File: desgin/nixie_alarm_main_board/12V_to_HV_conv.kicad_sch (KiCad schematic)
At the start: 23 parts, among them IC1 LM3488MM, IC8 MCP4018T-502E_LT, Q8 TPH5200FNH,L1Q

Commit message: koncepcja układu
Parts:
- IC8: value MCP4018T-502E_LT -> MCP4018T-103E/LT
- R44: value 27kΩ -> 35.7kΩ
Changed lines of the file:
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@@
 			)
 		)
-		(property "Value" "MCP4018T-502E_LT"
+		(property "Value" "MCP4018T-103E/LT"
 			(at 45.72 104.14 0)
 			(effects
@@
 			)
 		)
-		(property "Description" "5kΩ 7-bit"
+		(property "Description" "10kΩ 7-bit"
 			(at 45.974 118.872 0)
 			(effects
@@
 			)
 		)
-		(property "Value" "27kΩ"
+		(property "Value" "35.7kΩ"
 			(at 158.75 109.22 90)
 			(effects

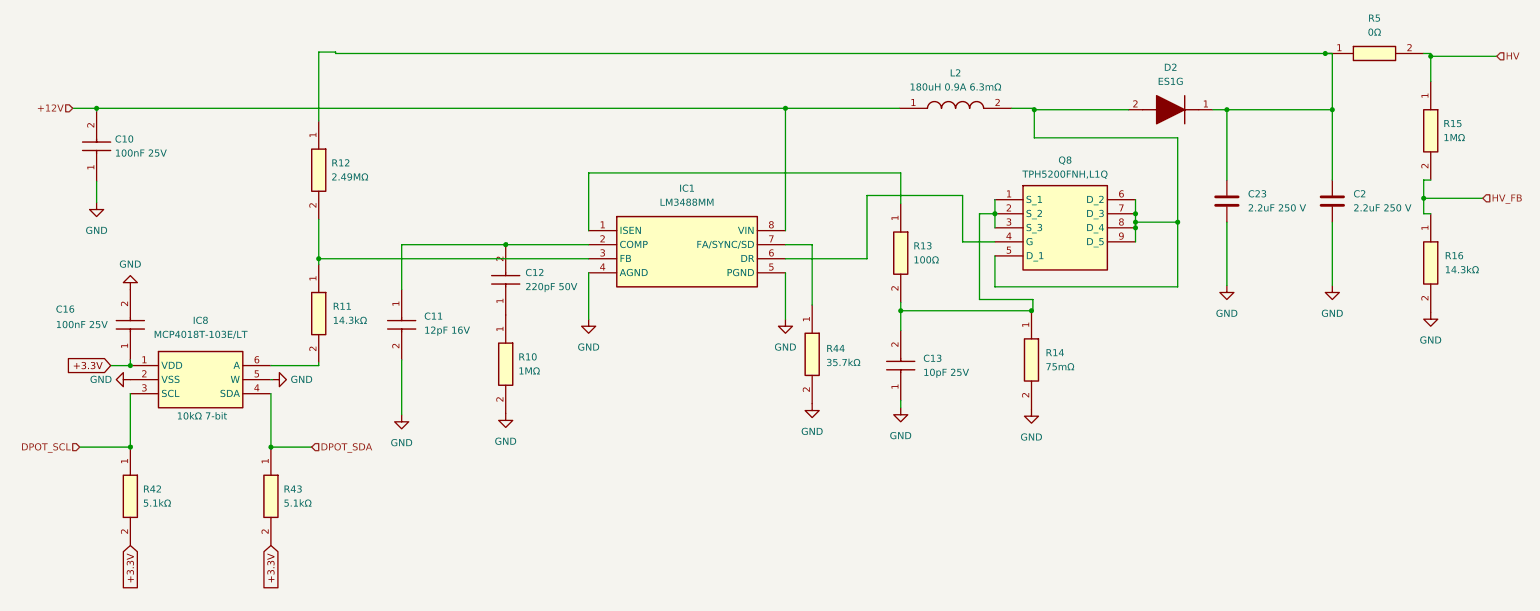
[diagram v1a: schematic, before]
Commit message: zener diode on fb
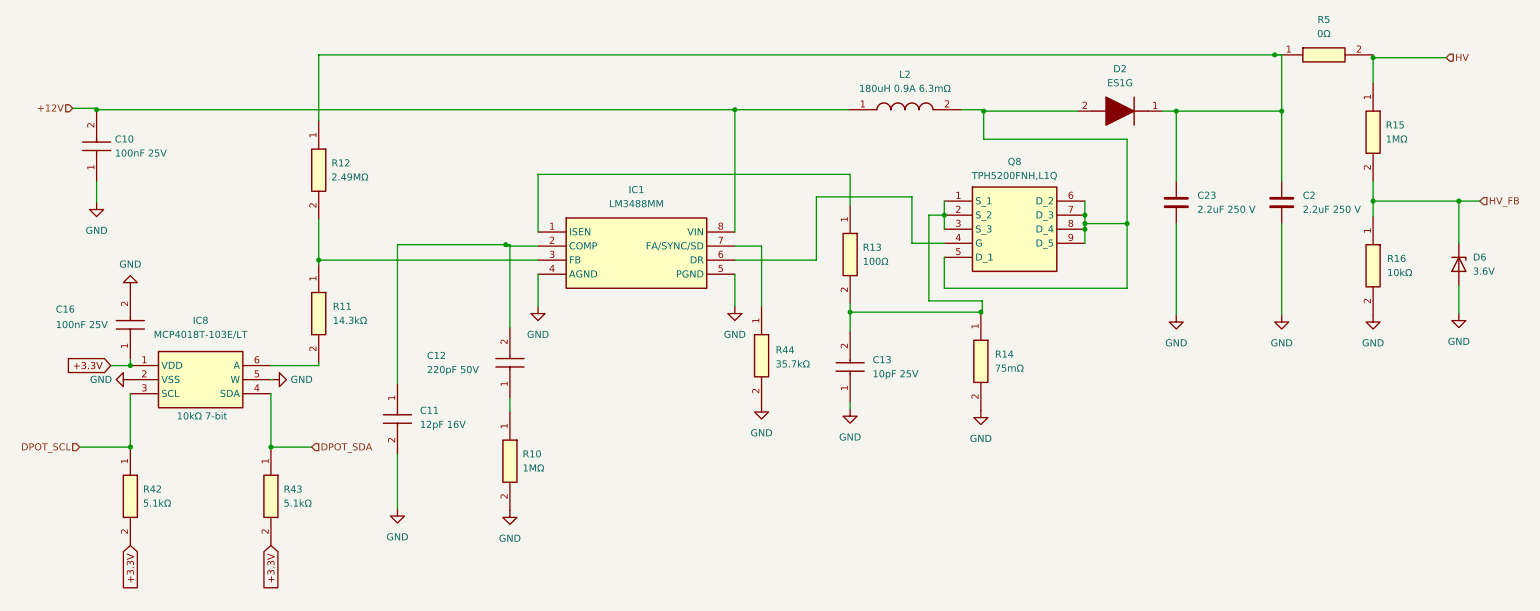
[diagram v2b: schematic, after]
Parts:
- added D6: 3.6V, Diode_SMD:D_0805_2012Metric_Pad1.15x1.40mm_HandSolder, symbol Device:D_Zener
- R16: value 14.3kΩ -> 10kΩ
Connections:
- net GND: now also D6.2 (A)
- net HV_FB: now also D6.1 (K)
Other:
- moved on the sheet: C11, C12, C13, C2, C23, D2, IC1, L2, Q8, R10, R13, R14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
